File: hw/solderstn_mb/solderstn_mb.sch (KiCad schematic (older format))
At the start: 0 parts

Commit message: Summer vacation 2020 updates: * Front panel design rev 1 complete (incl Experimental outer board with optional linear touch sensors) * MB schematics AlmostDone(tm) - 'old' pinout supporting only one Rotary encoder * Lots of docs for new stuff
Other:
- note added: "0010001 (if ~SEN~ pulled low [default])\n1100011 (alternative, if ~SEN~ pulled high)"
- note added: "1000000 (ch A, heater 1)\n1000001 (ch A, heater 2)\n1000100 (ch B, heater 1)\n1000101 (ch B, heater 2)"
- note added: "1001000 (Front panel, outside left)\n1001010 (FP, outside right)\n1001100 (FP, inside left)\n1001101 (FP, inside middle)\n1001110 (FP, inside right)\n1001001 (Main board #1)\n1001011 (MB #2)\n1001111 (MB #3)"
- note added: "I2C-addresses (on I2C1)"
- note added: "INA226 (power-channel current sensors) :"
- note added: "SI4735 (FM-radio rx) :"
- note added: "TMP100 (temperature sensors) :"
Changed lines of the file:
@@
 $Descr A4 11693 8268
 encoding utf-8
-Sheet 1 7
-Title ""
+Sheet 1 21
+Title "DIY Soldering station, top level"
 Date "2020-04-26"
 Rev "R0.1"
@@
 $EndDescr
 $Sheet
-S 1600 1000 1400 1400
-U 5EACD927
-F0 "STM32F429 MCU" 50
-F1 "mcu_1.sch" 50
-$EndSheet
-$Sheet
-S 1600 2800 1400 1400
+S 1550 4850 1400 1400
 U 5ED59CBF
 F0 "Ethernet" 50
@@
 $EndSheet
 $Sheet
-S 5000 1000 1400 1400
+S 1550 950  1400 1400
 U 5F472B62
 F0 "Power ctrl" 50
@@
 $EndSheet
 $Sheet
-S 3300 1000 1400 1400
+S 6100 1000 1400 1400
 U 5EAEB4B5
 F0 "STM32F429 PWR" 50
 F1 "mcu_2.sch" 50
+F2 "KTY_BIAS_EN" I L 6100 2250 50
+F3 "KTY_BIAS_CH_A" O R 7500 2050 50
+F4 "KTY_BIAS_CH_B" O R 7500 2250 50
 $EndSheet
 $Sheet
-S 3300 2800 1400 1400
+S 3800 950  1400 1400
 U 5F472FC2
 F0 "Front panel connections" 50
 F1 "front_panel_conn.sch" 50
+F2 "AUX_TX" O L 3800 2250 50
+F3 "AUX_RX" I L 3800 2150 50
 $EndSheet
 $Sheet
-S 5000 2800 1400 1400
+S 3800 4850 1400 1400
 U 5F4730B9
 F0 "Rear panel connections" 50
 F1 "rear_panel_conn.sch" 50
+F2 "CH_A_HEATER_1" I R 5200 5150 50
+F3 "CH_A_HEATER_2" I R 5200 5250 50
+F4 "CH_A_TC1" O R 5200 4950 50
+F5 "CH_A_TC2_KTY" O R 5200 5050 50
+F6 "CH_B_HEATER_1" I R 5200 5750 50
+F7 "CH_B_HEATER_2" I R 5200 5850 50
+F8 "CH_B_TC1" O R 5200 5550 50
+F9 "CH_B_TC2_KTY" O R 5200 5650 50
 $EndSheet
+$Sheet
+S 6100 2850 1400 1400
+U 5F785D6E
+F0 "Weller contol" 50
+F1 "Weller_ctrl.sch" 50
+F2 "KTY_BIAS_CH_A" I R 7500 3150 50
+F3 "KTY_BIAS_CH_B" I R 7500 2950 50
+F4 "CH_A_HEATER_1" O L 6100 3550 50
+F5 "CH_A_HEATER_2" O L 6100 3650 50
+F6 "CH_B_HEATER_1" O L 6100 4050 50
+F7 "CH_B_HEATER_2" O L 6100 4150 50
+F8 "CH_A_TC1" I L 6100 3350 50
+F9 "CH_A_TC2_KTY" I L 6100 3450 50
+F10 "CH_B_TC1" I L 6100 3850 50
+F11 "CH_B_TC2_KTY" I L 6100 3950 50
+$EndSheet
+$Sheet
+S 1550 2850 1400 1400
+U 5FAFD5BA
+F0 "Audio & FM-radio" 50
+F1 "audio_fmradio.sch" 50
+$EndSheet
+$Sheet
+S 3800 2850 1400 1400
+U 5EACD927
+F0 "STM32F429 MCU" 50
+F1 "mcu_1.sch" 50
+F2 "AUX_HOST_RX" I L 3800 2950 50
+F3 "AUX_HOST_TX" O L 3800 3050 50
+F4 "KTY_BIAS_ENABLE" O R 5200 2950 50
+$EndSheet
+Wire Wire Line
+	3800 2250 3650 2250
+Wire Wire Line
+	3650 2250 3650 2950
+Wire Wire Line
+	3650 2950 3800 2950
+Wire Wire Line
+	3800 2150 3550 2150
+Wire Wire Line
+	3550 2150 3550 3050
+Wire Wire Line
+	3550 3050 3800 3050
+Wire Wire Line
+	5200 2950 5650 2950
+Wire Wire Line
+	5650 2950 5650 2250
+Wire Wire Line
+	5650 2250 6100 2250
+Wire Wire Line
+	7500 2250 7650 2250
+Wire Wire Line
+	7650 2250 7650 2950
+Wire Wire Line
+	7650 2950 7500 2950
+Wire Wire Line
+	7500 2050 7800 2050
+Wire Wire Line
+	7800 2050 7800 3150
+Wire Wire Line
+	7800 3150 7500 3150
+Wire Wire Line
+	6100 3350 5400 3350
+Wire Wire Line
+	5400 3350 5400 4950
+Wire Wire Line
+	5400 4950 5200 4950
+Wire Wire Line
+	6100 3450 5500 3450
+Wire Wire Line
+	5500 3450 5500 5050
+Wire Wire Line
+	5500 5050 5200 5050
+Wire Wire Line
+	6100 3550 5600 3550
+Wire Wire Line
+	5600 3550 5600 5150
+Wire Wire Line
+	5600 5150 5200 5150
+Wire Wire Line
+	6100 3650 5700 3650
+Wire Wire Line
+	5700 3650 5700 5250
+Wire Wire Line
+	5700 5250 5200 5250
+Wire Wire Line
+	6100 3850 5750 3850
+Wire Wire Line
+	5750 3850 5750 5550
+Wire Wire Line
+	5750 5550 5200 5550
+Wire Wire Line
+	6100 3950 5850 3950
+Wire Wire Line
+	5850 3950 5850 5650
+Wire Wire Line
+	5850 5650 5200 5650
+Wire Wire Line
+	6100 4050 5950 4050
+Wire Wire Line
+	5950 4050 5950 5750
+Wire Wire Line
+	5950 5750 5200 5750
+Wire Wire Line
+	6100 4150 6050 4150
+Wire Wire Line
+	6050 4150 6050 5850
+Wire Wire Line
+	6050 5850 5200 5850
+Text Notes 9000 1100 0    70   Italic 14
+I2C-addresses (on I2C1)
+Text Notes 9100 1200 0    60   ~ 12
+TMP100 (temperature sensors) :
+Text Notes 9200 1900 0    50   ~ 10
+1001000 (Front panel, outside left)\n1001010 (FP, outside right)\n1001100 (FP, inside left)\n1001101 (FP, inside middle)\n1001110 (FP, inside right)\n1001001 (Main board #1)\n1001011 (MB #2)\n1001111 (MB #3)
+Text Notes 9100 2050 0    60   ~ 12
+INA226 (power-channel current sensors) :
+Text Notes 9200 2400 0    50   ~ 10
+1000000 (ch A, heater 1)\n1000001 (ch A, heater 2)\n1000100 (ch B, heater 1)\n1000101 (ch B, heater 2)
+Text Notes 9100 2550 0    60   ~ 12
+SI4735 (FM-radio rx) :
+Text Notes 9200 2750 0    50   ~ 10
+0010001 (if ~SEN~ pulled low [default])\n1100011 (alternative, if ~SEN~ pulled high)
 $EndSCHEMATC

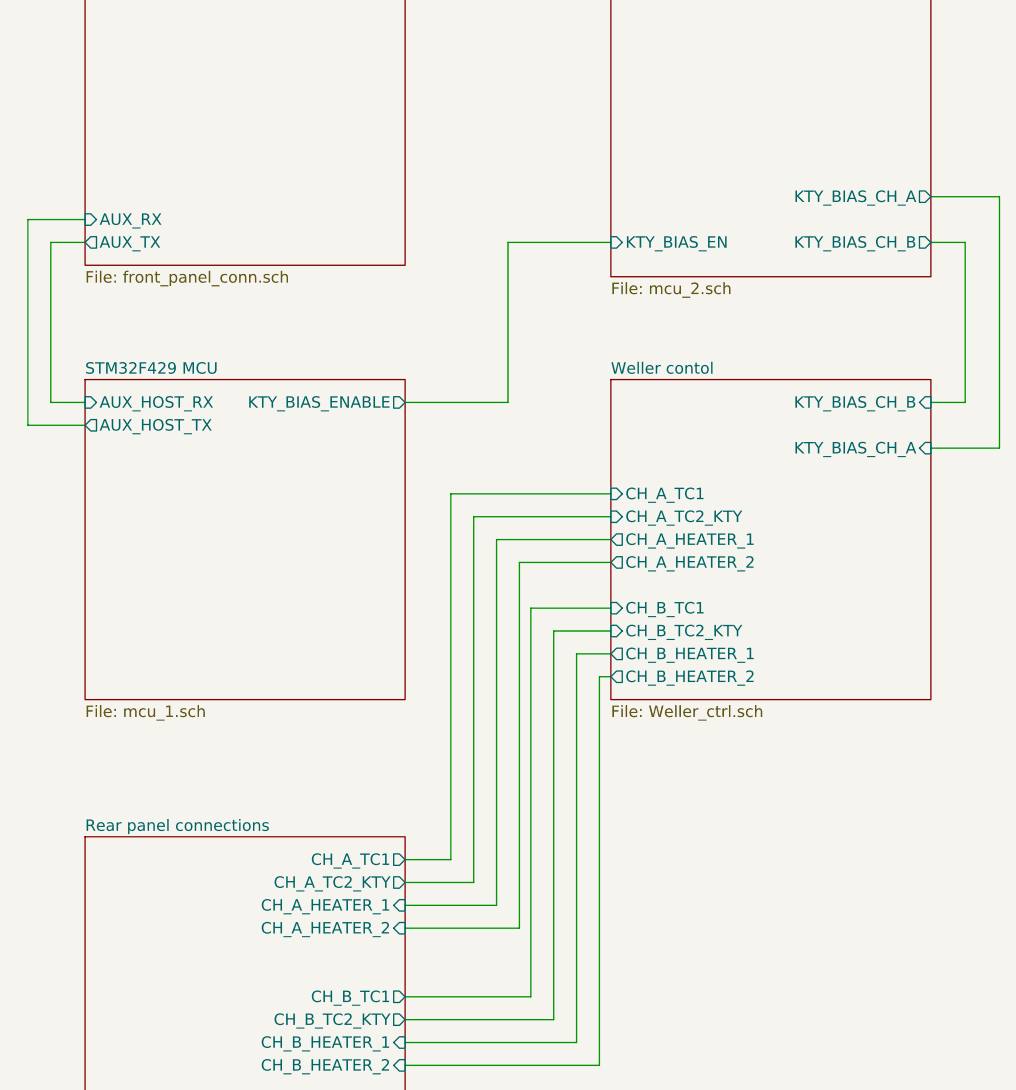
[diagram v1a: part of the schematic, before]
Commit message: Update pinout to "alternative", shuffling stuff around to optionally support a 2nd rotary on front-panel (corresponding Front-panel side not yet updated)
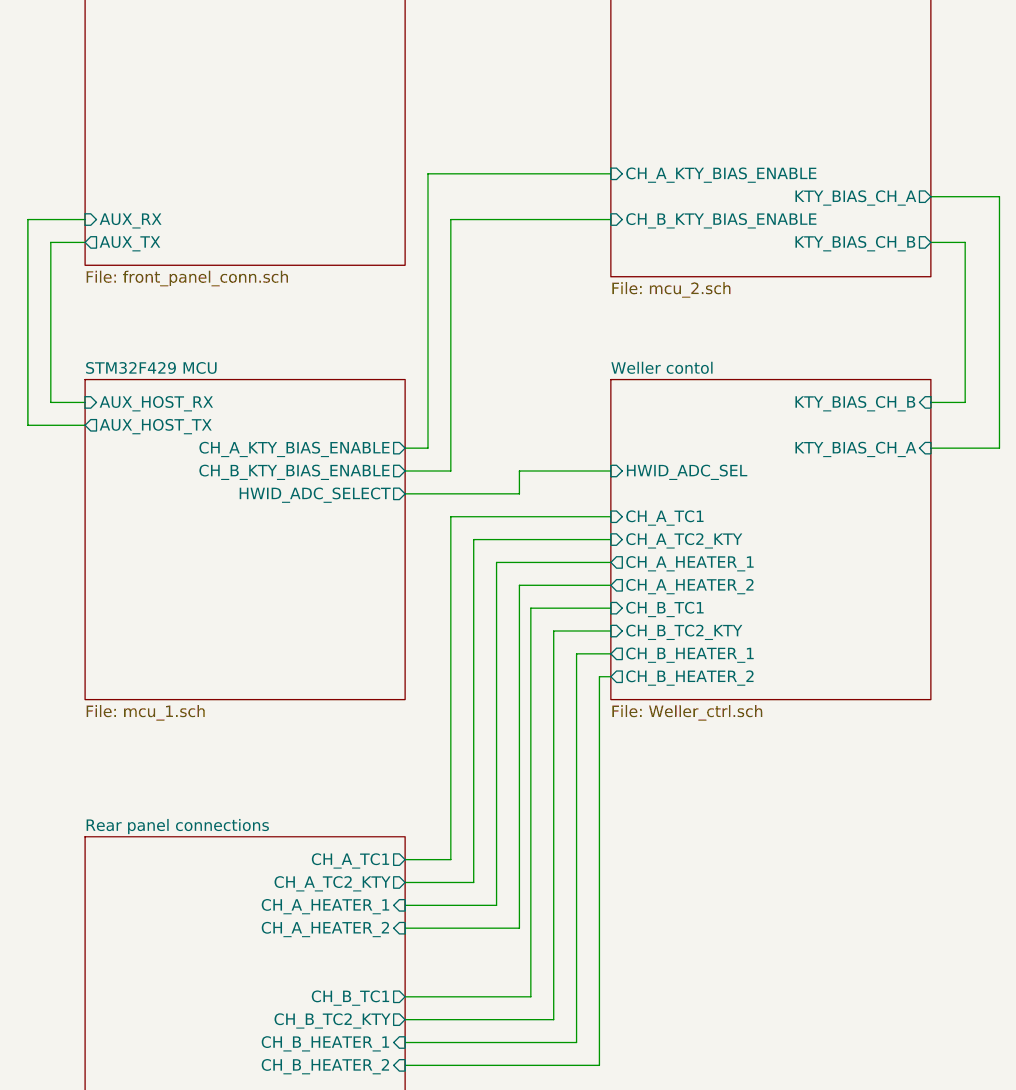
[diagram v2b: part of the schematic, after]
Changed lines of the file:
@@
 F0 "STM32F429 PWR" 50
 F1 "mcu_2.sch" 50
-F2 "KTY_BIAS_EN" I L 6100 2250 50
-F3 "KTY_BIAS_CH_A" O R 7500 2050 50
-F4 "KTY_BIAS_CH_B" O R 7500 2250 50
+F2 "KTY_BIAS_CH_A" O R 7500 2050 50
+F3 "KTY_BIAS_CH_B" O R 7500 2250 50
+F4 "CH_A_KTY_BIAS_ENABLE" I L 6100 1950 50
+F5 "CH_B_KTY_BIAS_ENABLE" I L 6100 2150 50
 $EndSheet
 $Sheet
@@
 F2 "KTY_BIAS_CH_A" I R 7500 3150 50
 F3 "KTY_BIAS_CH_B" I R 7500 2950 50
-F4 "CH_A_HEATER_1" O L 6100 3550 50
-F5 "CH_A_HEATER_2" O L 6100 3650 50
+F4 "CH_A_HEATER_1" O L 6100 3650 50
+F5 "CH_A_HEATER_2" O L 6100 3750 50
 F6 "CH_B_HEATER_1" O L 6100 4050 50
 F7 "CH_B_HEATER_2" O L 6100 4150 50
-F8 "CH_A_TC1" I L 6100 3350 50
-F9 "CH_A_TC2_KTY" I L 6100 3450 50
+F8 "CH_A_TC1" I L 6100 3450 50
+F9 "CH_A_TC2_KTY" I L 6100 3550 50
 F10 "CH_B_TC1" I L 6100 3850 50
 F11 "CH_B_TC2_KTY" I L 6100 3950 50
+F12 "HWID_ADC_SEL" I L 6100 3250 50
 $EndSheet
 $Sheet
@@
 F2 "AUX_HOST_RX" I L 3800 2950 50
 F3 "AUX_HOST_TX" O L 3800 3050 50
-F4 "KTY_BIAS_ENABLE" O R 5200 2950 50
+F4 "CH_A_KTY_BIAS_ENABLE" O R 5200 3150 50
+F5 "CH_B_KTY_BIAS_ENABLE" O R 5200 3250 50
+F6 "HWID_ADC_SELECT" O R 5200 3350 50
 $EndSheet
 Wire Wire Line
@@
 	3550 3050 3800 3050
 Wire Wire Line
-	5200 2950 5650 2950
-Wire Wire Line
-	5650 2950 5650 2250
-Wire Wire Line
-	5650 2250 6100 2250
-Wire Wire Line
 	7500 2250 7650 2250
 Wire Wire Line
@@
 	7800 3150 7500 3150
 Wire Wire Line
-	6100 3350 5400 3350
+	6100 3450 5400 3450
 Wire Wire Line
-	5400 3350 5400 4950
+	5400 3450 5400 4950
 Wire Wire Line
 	5400 4950 5200 4950
 Wire Wire Line
-	6100 3450 5500 3450
+	6100 3550 5500 3550
 Wire Wire Line
-	5500 3450 5500 5050
+	5500 3550 5500 5050
 Wire Wire Line
 	5500 5050 5200 5050
 Wire Wire Line
-	6100 3550 5600 3550
+	6100 3650 5600 3650
 Wire Wire Line
-	5600 3550 5600 5150
+	5600 3650 5600 5150
 Wire Wire Line
 	5600 5150 5200 5150
 Wire Wire Line
-	6100 3650 5700 3650
+	6100 3750 5700 3750
 Wire Wire Line
-	5700 3650 5700 5250
+	5700 3750 5700 5250
 Wire Wire Line
 	5700 5250 5200 5250
@@
 Text Notes 9200 2750 0    50   ~ 10
 0010001 (if ~SEN~ pulled low [default])\n1100011 (alternative, if ~SEN~ pulled high)
+Wire Wire Line
+	5200 3150 5300 3150
+Wire Wire Line
+	5300 3150 5300 1950
+Wire Wire Line
+	5300 1950 6100 1950
+Wire Wire Line
+	5200 3250 5400 3250
+Wire Wire Line
+	5400 3250 5400 2150
+Wire Wire Line
+	5400 2150 6100 2150
+Wire Wire Line
+	5200 3350 5700 3350
+Wire Wire Line
+	5700 3350 5700 3250
+Wire Wire Line
+	5700 3250 6100 3250
 $EndSCHEMATC

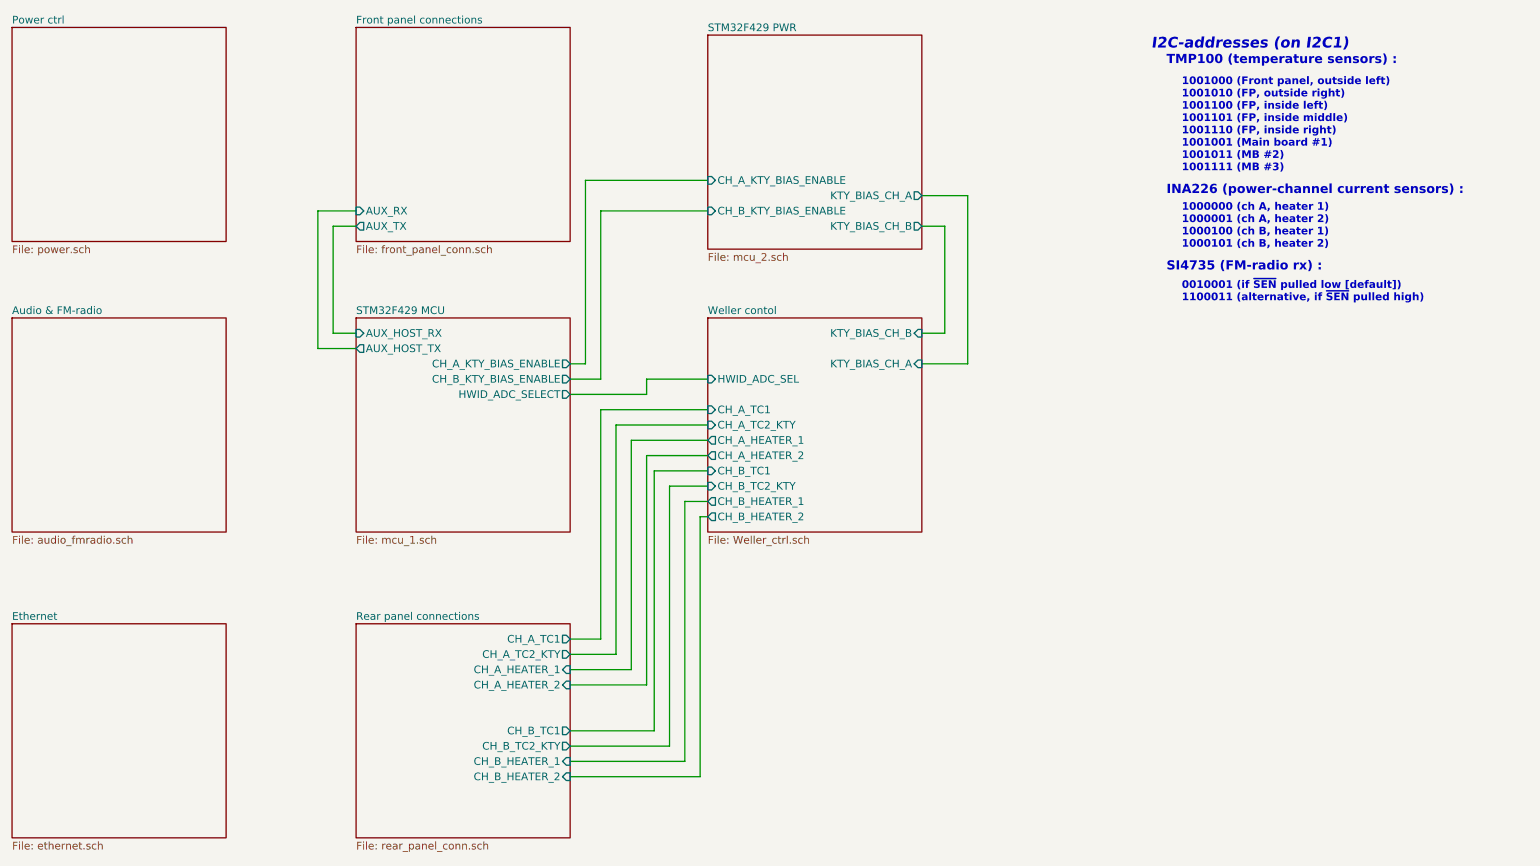
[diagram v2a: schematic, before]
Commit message: * Remove separate REED_PULLUP_EN pin; instead bias the Reedswitches with the per-channel KTY bias (buffered Vref) * Add separate mini cut-out sub-PCB for 3.5 headphone connector at back-panel (must be angled vertical to fit in panel) * Some ESD and buffering on back panel
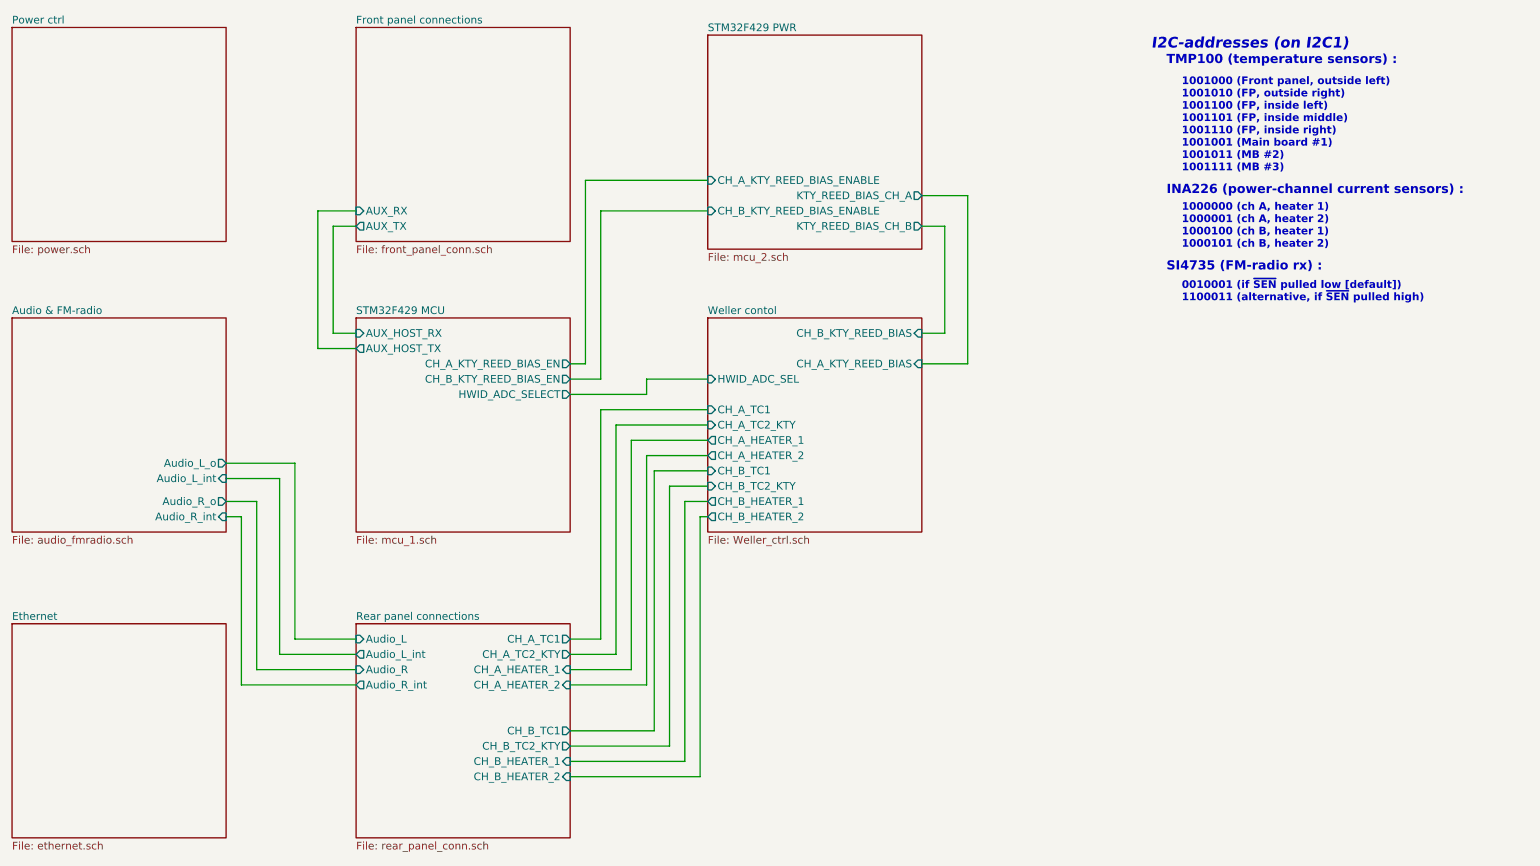
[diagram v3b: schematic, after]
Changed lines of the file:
@@
 $Descr A4 11693 8268
 encoding utf-8
-Sheet 1 21
+Sheet 1 22
 Title "DIY Soldering station, top level"
 Date "2020-04-26"
@@
 F0 "STM32F429 PWR" 50
 F1 "mcu_2.sch" 50
-F2 "KTY_BIAS_CH_A" O R 7500 2050 50
-F3 "KTY_BIAS_CH_B" O R 7500 2250 50
-F4 "CH_A_KTY_BIAS_ENABLE" I L 6100 1950 50
-F5 "CH_B_KTY_BIAS_ENABLE" I L 6100 2150 50
+F2 "CH_A_KTY_REED_BIAS_ENABLE" I L 6100 1950 50
+F3 "KTY_REED_BIAS_CH_A" O R 7500 2050 50
+F4 "KTY_REED_BIAS_CH_B" O R 7500 2250 50
+F5 "CH_B_KTY_REED_BIAS_ENABLE" I L 6100 2150 50
 $EndSheet
 $Sheet
@@
 F8 "CH_B_TC1" O R 5200 5550 50
 F9 "CH_B_TC2_KTY" O R 5200 5650 50
+F10 "Audio_L" I L 3800 4950 50
+F11 "Audio_L_int" O L 3800 5050 50
+F12 "Audio_R" I L 3800 5150 50
+F13 "Audio_R_int" O L 3800 5250 50
 $EndSheet
 $Sheet
@@
 F0 "Weller contol" 50
 F1 "Weller_ctrl.sch" 50
-F2 "KTY_BIAS_CH_A" I R 7500 3150 50
-F3 "KTY_BIAS_CH_B" I R 7500 2950 50
-F4 "CH_A_HEATER_1" O L 6100 3650 50
-F5 "CH_A_HEATER_2" O L 6100 3750 50
-F6 "CH_B_HEATER_1" O L 6100 4050 50
-F7 "CH_B_HEATER_2" O L 6100 4150 50
-F8 "CH_A_TC1" I L 6100 3450 50
-F9 "CH_A_TC2_KTY" I L 6100 3550 50
-F10 "CH_B_TC1" I L 6100 3850 50
-F11 "CH_B_TC2_KTY" I L 6100 3950 50
-F12 "HWID_ADC_SEL" I L 6100 3250 50
+F2 "CH_A_HEATER_1" O L 6100 3650 50
+F3 "CH_A_HEATER_2" O L 6100 3750 50
+F4 "CH_B_HEATER_1" O L 6100 4050 50
+F5 "CH_B_HEATER_2" O L 6100 4150 50
+F6 "CH_A_TC1" I L 6100 3450 50
+F7 "CH_A_TC2_KTY" I L 6100 3550 50
+F8 "CH_B_TC1" I L 6100 3850 50
+F9 "CH_B_TC2_KTY" I L 6100 3950 50
+F10 "HWID_ADC_SEL" I L 6100 3250 50
+F11 "CH_A_KTY_REED_BIAS" I R 7500 3150 50
+F12 "CH_B_KTY_REED_BIAS" I R 7500 2950 50
 $EndSheet
 $Sheet
@@
 F0 "Audio & FM-radio" 50
 F1 "audio_fmradio.sch" 50
+F2 "Audio_R_o" O R 2950 4050 50
+F3 "Audio_L_o" O R 2950 3800 50
+F4 "Audio_R_int" I R 2950 4150 50
+F5 "Audio_L_int" I R 2950 3900 50
 $EndSheet
 $Sheet
@@
 F2 "AUX_HOST_RX" I L 3800 2950 50
 F3 "AUX_HOST_TX" O L 3800 3050 50
-F4 "CH_A_KTY_BIAS_ENABLE" O R 5200 3150 50
-F5 "CH_B_KTY_BIAS_ENABLE" O R 5200 3250 50
-F6 "HWID_ADC_SELECT" O R 5200 3350 50
+F4 "HWID_ADC_SELECT" O R 5200 3350 50
+F5 "CH_A_KTY_REED_BIAS_EN" O R 5200 3150 50
+F6 "CH_B_KTY_REED_BIAS_EN" O R 5200 3250 50
 $EndSheet
 Wire Wire Line
@@
 Wire Wire Line
 	5700 3250 6100 3250
+Wire Wire Line
+	2950 4150 3050 4150
+Wire Wire Line
+	3050 4150 3050 5250
+Wire Wire Line
+	3050 5250 3800 5250
+Wire Wire Line
+	2950 4050 3150 4050
+Wire Wire Line
+	3150 4050 3150 5150
+Wire Wire Line
+	3150 5150 3800 5150
+Wire Wire Line
+	2950 3900 3300 3900
+Wire Wire Line
+	3300 3900 3300 5050
+Wire Wire Line
+	3300 5050 3800 5050
+Wire Wire Line
+	2950 3800 3400 3800
+Wire Wire Line
+	3400 3800 3400 4950
+Wire Wire Line
+	3400 4950 3800 4950
 $EndSCHEMATC
